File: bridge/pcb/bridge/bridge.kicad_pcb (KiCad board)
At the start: 2 copper layers, 108 x 80 mm, 44 parts, among them J1 Screw_Terminal_01x06, J2 Screw_Terminal_01x06, J3 Screw_Terminal_01x06, J4 Conn_01x23, J5 Conn_01x04, J6 Conn_01x02, J7 Conn_01x03, J8 Conn_01x02, J9 MCU_Test_Point, SW1 SW_SPST, SW2 SW_SPST, SW3 SW_SPST, SW4 SW_SPST, U1 L293, U2 J104D2C12VDC.20S, U4 ATmega328P-P, U5 L7805, U6 MCP4901

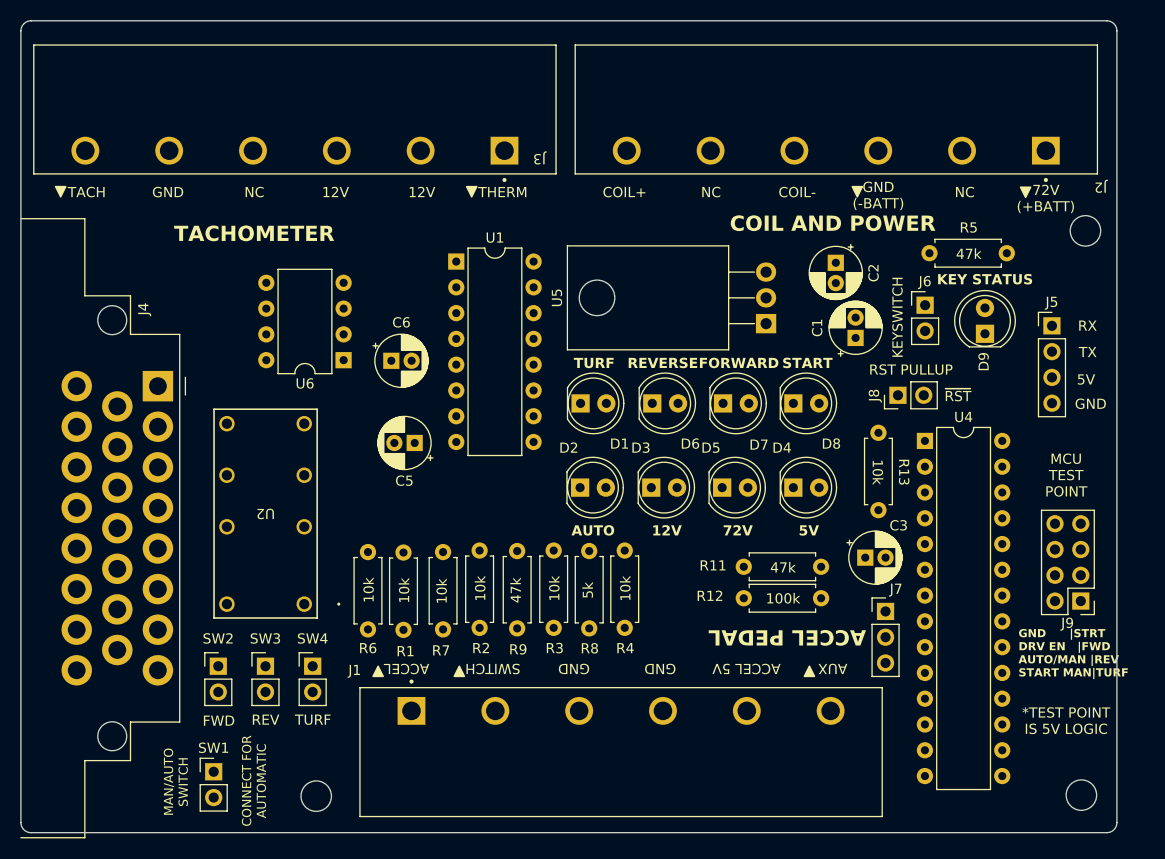
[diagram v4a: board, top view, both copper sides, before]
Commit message: Improved connector labeling and added more detail
Labeled wiper 1 and wiper 2 for accel pedal

Changed +/- to be before COIL instead of after i.e. "-COIL" instead of "COIL-"
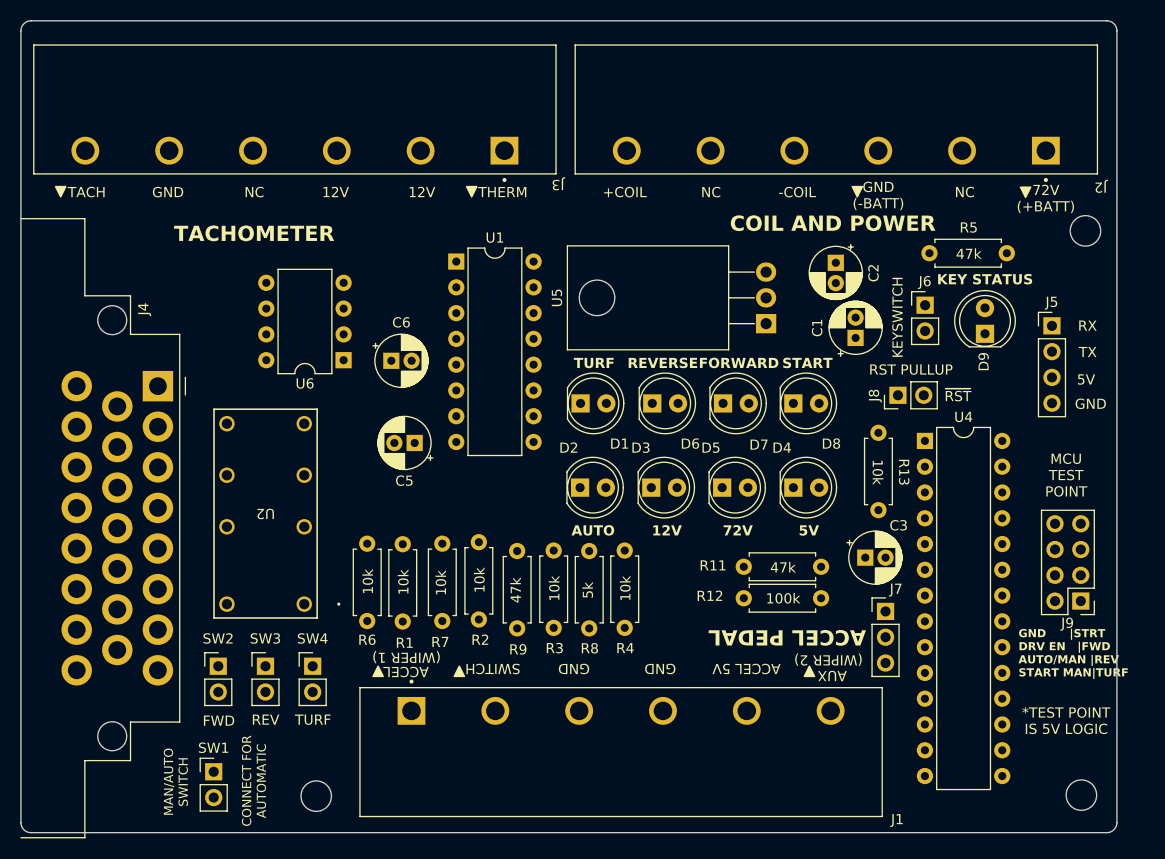
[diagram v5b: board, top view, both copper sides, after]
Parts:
- moved R1 0.83 mm to (100.7, 96.3)
- moved R2 0.83 mm to (108.2, 96.1)
- moved R7 0.83 mm to (104.4, 96.4)
- moved R6 0.83 mm to (97.2, 96.3)
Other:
- board text added: "(WIPER 1)"
- board text added: "(WIPER 2)"
- board text added: "+COIL"
- board text added: "-COIL"
- board text removed: "COIL+"
- board text removed: "COIL-"
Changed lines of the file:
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@@
   )
   (footprint "bridge:THT_RESISTOR_WITH_VALUE" (layer "F.Cu")
-    (at 108.3 96.95 90)
+    (at 108.225 96.125 90)
     (property "Sheetfile" "mcu.kicad_sch")
     (property "Sheetname" "MCU")
@@
   )
   (footprint "bridge:THT_RESISTOR_WITH_VALUE" (layer "F.Cu")
-    (at 104.5 97.22 -90)
+    (at 104.425 96.395 -90)
     (property "Sheetfile" "bridge.kicad_sch")
     (property "Sheetname" "")
@@
   )
   (footprint "bridge:THT_RESISTOR_WITH_VALUE" (layer "F.Cu")
-    (at 100.8 97.15 90)
+    (at 100.725 96.325 90)
     (property "Sheetfile" "mcu.kicad_sch")
     (property "Sheetname" "MCU")
@@
   )
   (footprint "bridge:THT_RESISTOR_WITH_VALUE" (layer "F.Cu")
-    (at 97.3 97.1 90)
+    (at 97.225 96.275 90)
     (property "Sheetfile" "bridge.kicad_sch")
     (property "Sheetname" "")
@@
     (property "ki_keywords" "screw terminal")
     (attr through_hole)
-    (fp_text reference "J1" (at -5.484 -4 unlocked) (layer "F.SilkS")
+    (fp_text reference "J1" (at 47.991 10.7 unlocked) (layer "F.SilkS")
         (effects (font (size 1 1) (thickness 0.1)))
     )
@@
     (property "ki_keywords" "screw terminal")
     (attr through_hole)
-    (fp_text reference "J3" (at -3.344 -0.8025 180 unlocked) (layer "F.SilkS")
+    (fp_text reference "J3" (at -5.169 -3.3525 180 unlocked) (layer "F.SilkS")
         (effects (font (size 1 1) (thickness 0.1)))
     )
@@
     (effects (font (size 1 1) (thickness 0.15)) (justify bottom))
   )
-  (gr_text "COIL+" (at 122.5 58.5) (layer "F.SilkS")
+  (gr_text "+COIL" (at 122.5 58.5) (layer "F.SilkS")
     (effects (font (size 1 1) (thickness 0.15)) (justify bottom))
   )
@@
     (effects (font (size 1.5 1.5) (thickness 0.3) bold))
   )
+  (gr_text "(WIPER 2)" (at 142.575 103.4 180) (layer "F.SilkS")
+    (effects (font (size 1 1) (thickness 0.15)) (justify bottom))
+  )
   (gr_text "12V" (at 102.5 58.5) (layer "F.SilkS")
     (effects (font (size 1 1) (thickness 0.15)) (justify bottom))
   )
-  (gr_text "COIL-" (at 139.5 58.5) (layer "F.SilkS")
+  (gr_text "-COIL" (at 139.5 58.5) (layer "F.SilkS")
     (effects (font (size 1 1) (thickness 0.15)) (justify bottom))
   )
@@
     (effects (font (size 1 1) (thickness 0.15)) (justify bottom))
   )
-  (gr_text "ACCEL" (at 101 104.25 180) (layer "F.SilkS")
+  (gr_text "ACCEL" (at 100.95 104.55 180) (layer "F.SilkS")
     (effects (font (size 1 1) (thickness 0.15)) (justify bottom))
   )
@@
     (effects (font (size 1 1) (thickness 0.15)) (justify bottom))
   )
+  (gr_text "(WIPER 1)" (at 101 103.15 180) (layer "F.SilkS")
+    (effects (font (size 1 1) (thickness 0.15)) (justify bottom))
+  )
   (gr_text "NC" (at 86 58.5) (layer "F.SilkS")
     (effects (font (size 1 1) (thickness 0.15)) (justify bottom))
@@
     (effects (font (size 1 1) (thickness 0.15)))
   )
-  (gr_text "AUX" (at 143 104.25 180) (layer "F.SilkS")
+  (gr_text "AUX" (at 142.95 104.95 180) (layer "F.SilkS")
     (effects (font (size 1 1) (thickness 0.15)) (justify bottom))
   )

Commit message: Adjusted LED colors
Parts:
- D1, D6, D7, D8: value GREEN -> YELLOW
- D2: value YELLOW -> BLUE
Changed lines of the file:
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@@
         (effects (font (size 1 1) (thickness 0.15)))
     )
-    (fp_text value "GREEN" (at 1.27 3.96) (layer "F.Fab")
+    (fp_text value "YELLOW" (at 1.27 3.96) (layer "F.Fab")
         (effects (font (size 1 1) (thickness 0.15)))
     )
@@
         (effects (font (size 1 1) (thickness 0.15)))
     )
-    (fp_text value "YELLOW" (at 1.27 3.96) (layer "F.Fab")
+    (fp_text value "BLUE" (at 1.27 3.96) (layer "F.Fab")
         (effects (font (size 1 1) (thickness 0.15)))
     )
@@
         (effects (font (size 1 1) (thickness 0.15)))
     )
-    (fp_text value "GREEN" (at 1.27 3.96) (layer "F.Fab")
+    (fp_text value "YELLOW" (at 1.27 3.96) (layer "F.Fab")
         (effects (font (size 1 1) (thickness 0.15)))
     )
@@
         (effects (font (size 1 1) (thickness 0.15)))
     )
-    (fp_text value "GREEN" (at 1.27 3.96) (layer "F.Fab")
+    (fp_text value "YELLOW" (at 1.27 3.96) (layer "F.Fab")
         (effects (font (size 1 1) (thickness 0.15)))
     )
@@
         (effects (font (size 1 1) (thickness 0.15)))
     )
-    (fp_text value "GREEN" (at 1.27 3.96) (layer "F.Fab")
-        (effects (font (size 1 1) (thickness 0.15)))
-    )
+    (fp_text value "YELLOW" (at 1.27 3.96) (layer "F.Fab")
+        (effects (font (size 1 1) (thickness 0.15)))
+    )

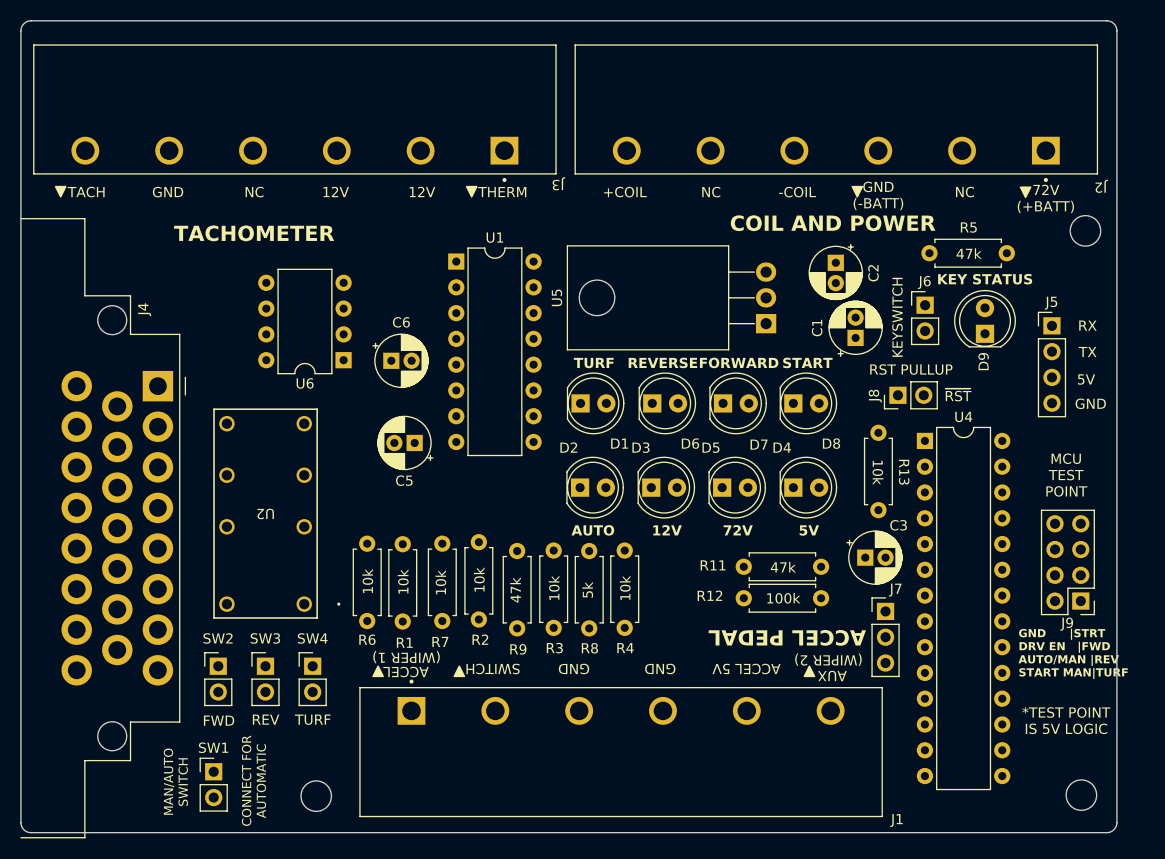
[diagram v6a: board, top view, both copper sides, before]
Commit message: Added switch for contactor coil, adjusted labeling
Slightly changed labels for the KEY and MAN/AUTO switches
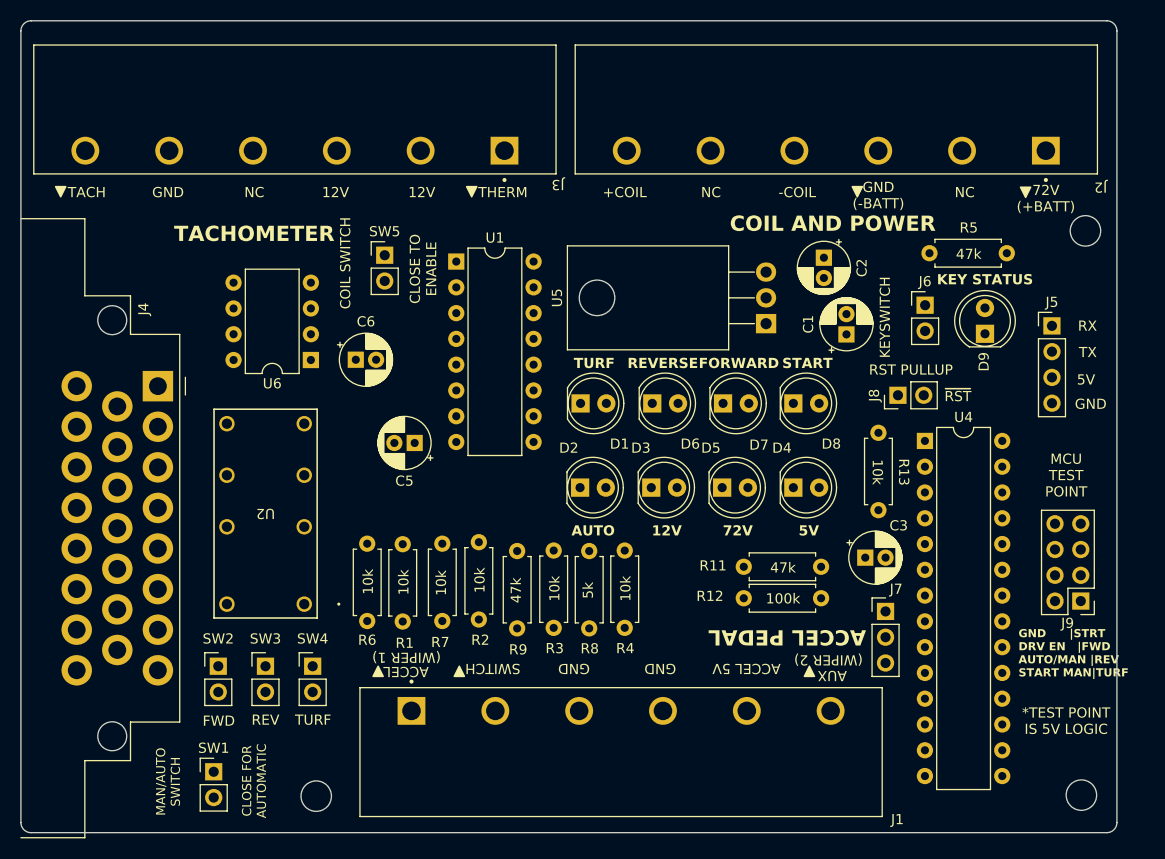
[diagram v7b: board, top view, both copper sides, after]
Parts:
- added SW5: SW_SPST, Connector_PinHeader_2.54mm:PinHeader_1x02_P2.54mm_Vertical, F.Cu at (98.8, 64.1)
- moved C6 3.50 mm to (96.0, 74.4)
- moved U6 3.23 mm to (91.6, 74.4)
- moved C2 1.28 mm to (142.1, 64.3)
- moved C1 0.97 mm to (144.3, 71.9)
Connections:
- J2 pad 6: +BATT -> Net-(J2-Pin_6)
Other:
- board text added: "CLOSE FOR AUTOMATIC"
- board text added: "CLOSE TO ENABLE"
- board text added: "COIL SWITCH"
- board text removed: "CONNECT FOR AUTOMATIC"
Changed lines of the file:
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@@
   (net 62 "Net-(D9-A)")
   (net 63 "ACCEL_POT_5V")
+  (net 64 "Net-(J2-Pin_6)")
   (footprint "LED_THT:LED_D5.0mm" (layer "F.Cu")
     (at 125.215 78.7)
@@
       (net 10 "unconnected-(J2-Pin_5-Pad5)") (pinfunction "Pin_5") (pintype "passive+no_connect") (solder_mask_margin 0.102))
     (pad "6" thru_hole circle (at 41.406 0 180) (size 2.745 2.745) (drill 1.83) (layers "*.Cu" "*.Mask")
-      (net 7 "+BATT") (pinfunction "Pin_6") (pintype "passive") (solder_mask_margin 0.102))
+      (net 64 "Net-(J2-Pin_6)") (pinfunction "Pin_6") (pintype "passive") (solder_mask_margin 0.102))
     (model "${KIPRJMOD}/3d-models/TERMINAL HEADER 6P.step"
       (offset (xyz 20.75 -8.5 0))
@@
   )
   (footprint "Capacitor_THT:CP_Radial_D5.0mm_P2.00mm" (layer "F.Cu")
-    (at 143.3 64.8449 -90)
+    (at 142.125 64.344888 -90)
     (descr "CP, Radial series, Radial, pin pitch=2.00mm, , diameter=5mm, Electrolytic Capacitor")
     (tags "CP Radial series Radial pin pitch 2.00mm  diameter 5mm Electrolytic Capacitor")
@@
   )
   (footprint "Capacitor_THT:CP_Radial_D5.0mm_P2.00mm" (layer "F.Cu")
-    (at 99.5 74.5)
+    (at 96 74.4)
     (descr "CP, Radial series, Radial, pin pitch=2.00mm, , diameter=5mm, Electrolytic Capacitor")
     (tags "CP Radial series Radial pin pitch 2.00mm  diameter 5mm Electrolytic Capacitor")
@@
   )
   (footprint "Package_DIP:DIP-8_W7.62mm" (layer "F.Cu")
-    (at 94.8 74.44 180)
+    (at 91.575 74.425 180)
     (descr "8-lead though-hole mounted DIP package, row spacing 7.62 mm (300 mils)")
     (tags "THT DIP DIL PDIP 2.54mm 7.62mm 300mil")
@@
   )
   (footprint "Capacitor_THT:CP_Radial_D5.0mm_P2.00mm" (layer "F.Cu")
-    (at 145.25 72.25 90)
+    (at 144.35 71.9 90)
     (descr "CP, Radial series, Radial, pin pitch=2.00mm, , diameter=5mm, Electrolytic Capacitor")
     (tags "CP Radial series Radial pin pitch 2.00mm  diameter 5mm Electrolytic Capacitor")
@@
   )
   (footprint "Connector_PinHeader_2.54mm:PinHeader_1x02_P2.54mm_Vertical" (layer "F.Cu")
+    (at 98.85 64.1)
+    (descr "Through hole straight pin header, 1x02, 2.54mm pitch, single row")
+    (tags "Through hole pin header THT 1x02 2.54mm single row")
+    (property "Sheetfile" "bridge.kicad_sch")
+    (property "Sheetname" "")
+    (property "ki_description" "Single Pole Single Throw (SPST) switch")
+    (property "ki_keywords" "switch lever")
+    (attr through_hole)
+    (fp_text reference "SW5" (at 0 -2.33) (layer "F.SilkS")
+        (effects (font (size 1 1) (thickness 0.15)))
+    )
+    (fp_text value "SW_SPST" (at 0 4.87) (layer "F.Fab")
+        (effects (font (size 1 1) (thickness 0.15)))
+    )
+    (fp_text user "${REFERENCE}" (at 0 1.27 90) (layer "F.Fab")
+        (effects (font (size 1 1) (thickness 0.15)))
+    )
+    (fp_line (start -1.33 -1.33) (end 0 -1.33)
+      (stroke (width 0.12) (type solid)) (layer "F.SilkS"))
+    (fp_line (start -1.33 0) (end -1.33 -1.33)
+      (stroke (width 0.12) (type solid)) (layer "F.SilkS"))
+    (fp_line (start -1.33 1.27) (end -1.33 3.87)
+      (stroke (width 0.12) (type solid)) (layer "F.SilkS"))
+    (fp_line (start -1.33 1.27) (end 1.33 1.27)
+      (stroke (width 0.12) (type solid)) (layer "F.SilkS"))
+    (fp_line (start -1.33 3.87) (end 1.33 3.87)
+      (stroke (width 0.12) (type solid)) (layer "F.SilkS"))
+    (fp_line (start 1.33 1.27) (end 1.33 3.87)
+      (stroke (width 0.12) (type solid)) (layer "F.SilkS"))
+    (fp_line (start -1.8 -1.8) (end -1.8 4.35)
+      (stroke (width 0.05) (type solid)) (layer "F.CrtYd"))
+    (fp_line (start -1.8 4.35) (end 1.8 4.35)
+      (stroke (width 0.05) (type solid)) (layer "F.CrtYd"))
+    (fp_line (start 1.8 -1.8) (end -1.8 -1.8)
+      (stroke (width 0.05) (type solid)) (layer "F.CrtYd"))
+    (fp_line (start 1.8 4.35) (end 1.8 -1.8)
+      (stroke (width 0.05) (type solid)) (layer "F.CrtYd"))
+    (fp_line (start -1.27 -0.635) (end -0.635 -1.27)
+      (stroke (width 0.1) (type solid)) (layer "F.Fab"))
+    (fp_line (start -1.27 3.81) (end -1.27 -0.635)
+      (stroke (width 0.1) (type solid)) (layer "F.Fab"))
+    (fp_line (start -0.635 -1.27) (end 1.27 -1.27)
+      (stroke (width 0.1) (type solid)) (layer "F.Fab"))
+    (fp_line (start 1.27 -1.27) (end 1.27 3.81)
+      (stroke (width 0.1) (type solid)) (layer "F.Fab"))
+    (fp_line (start 1.27 3.81) (end -1.27 3.81)
+      (stroke (width 0.1) (type solid)) (layer "F.Fab"))
+    (pad "1" thru_hole rect (at 0 0) (size 1.7 1.7) (drill 1) (layers "*.Cu" "*.Mask")
+      (net 64 "Net-(J2-Pin_6)") (pinfunction "A") (pintype "passive"))
+    (pad "2" thru_hole oval (at 0 2.54) (size 1.7 1.7) (drill 1) (layers "*.Cu" "*.Mask")
+      (net 7 "+BATT") (pinfunction "B") (pintype "passive"))
+    (model "${KICAD6_3DMODEL_DIR}/Connector_PinHeader_2.54mm.3dshapes/PinHeader_1x02_P2.54mm_Vertical.wrl"
+      (offset (xyz 0 0 0))
+      (scale (xyz 1 1 1))
+      (rotate (xyz 0 0 0))
+    )
+  )
+  (footprint "Connector_PinHeader_2.54mm:PinHeader_1x02_P2.54mm_Vertical" (layer "F.Cu")
     (at 82 115)
     (descr "Through hole straight pin header, 1x02, 2.54mm pitch, single row")
@@
     (effects (font (size 1 1) (thickness 0.15)) (justify left bottom))
   )
-  (gr_text "KEYSWITCH" (at 150 74.25 90) (layer "F.SilkS")
+  (gr_text "KEYSWITCH" (at 148.75 74.25 90) (layer "F.SilkS")
     (effects (font (size 1 1) (thickness 0.125)) (justify left bottom))
   )
@@
     (effects (font (size 1 1) (thickness 0.2) bold))
   )
-  (gr_text "MAN/AUTO\nSWITCH" (at 78.3 116 90) (layer "F.SilkS")
+  (gr_text "MAN/AUTO\nSWITCH" (at 77.525 115.975 90) (layer "F.SilkS")
     (effects (font (size 0.9 0.9) (thickness 0.15)))
   )
@@
     (effects (font (size 1 1) (thickness 0.15)) (justify bottom))
   )
+  (gr_text "CLOSE TO\nENABLE" (at 104.05 65.45 90) (layer "F.SilkS")
+    (effects (font (size 1 1) (thickness 0.15)) (justify bottom))
+  )
   (gr_text "TACHOMETER" (at 86 62) (layer "F.SilkS")
     (effects (font (size 1.5 1.5) (thickness 0.3) bold))
@@
     (effects (font (size 1 1) (thickness 0.15)) (justify bottom))
   )
-  (gr_text "CONNECT FOR\nAUTOMATIC" (at 86 115.9 90) (layer "F.SilkS")
+  (gr_text "CLOSE FOR\nAUTOMATIC" (at 86 115.9 90) (layer "F.SilkS")
     (effects (font (size 0.9 0.9) (thickness 0.15)))
   )
@@
     (effects (font (size 1 1) (thickness 0.15)) (justify bottom))
   )
+  (gr_text "COIL SWITCH" (at 95.575 64.875 90) (layer "F.SilkS")
+    (effects (font (size 1 1) (thickness 0.15)) (justify bottom))
+  )
